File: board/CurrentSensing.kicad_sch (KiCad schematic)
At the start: 12 parts, among them U16 MLX91221KDF-ABF-025-RE, U17 MLX91221KDF-ABF-025-RE, U18 MLX91221KDF-ABF-025-RE

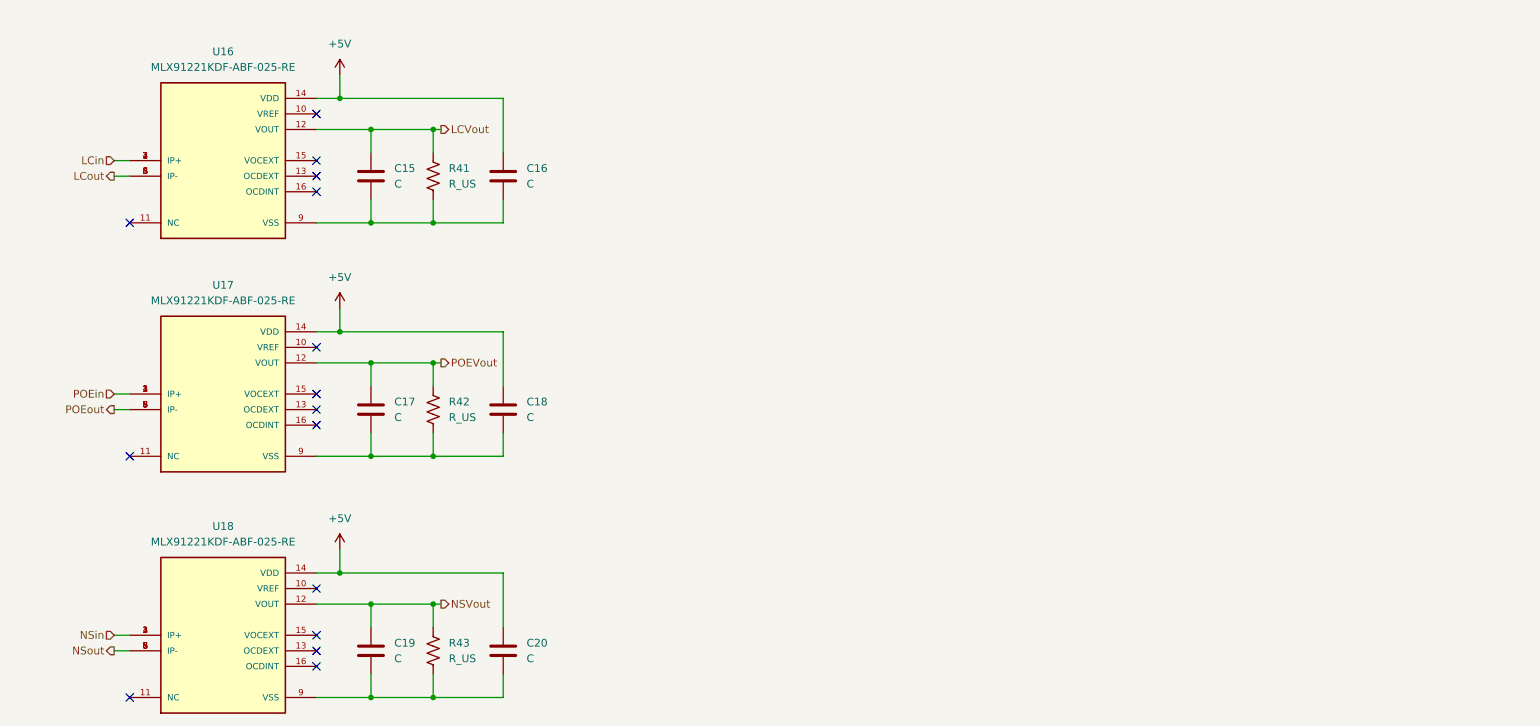
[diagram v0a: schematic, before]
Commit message: sync previous 2 commits changes correctly
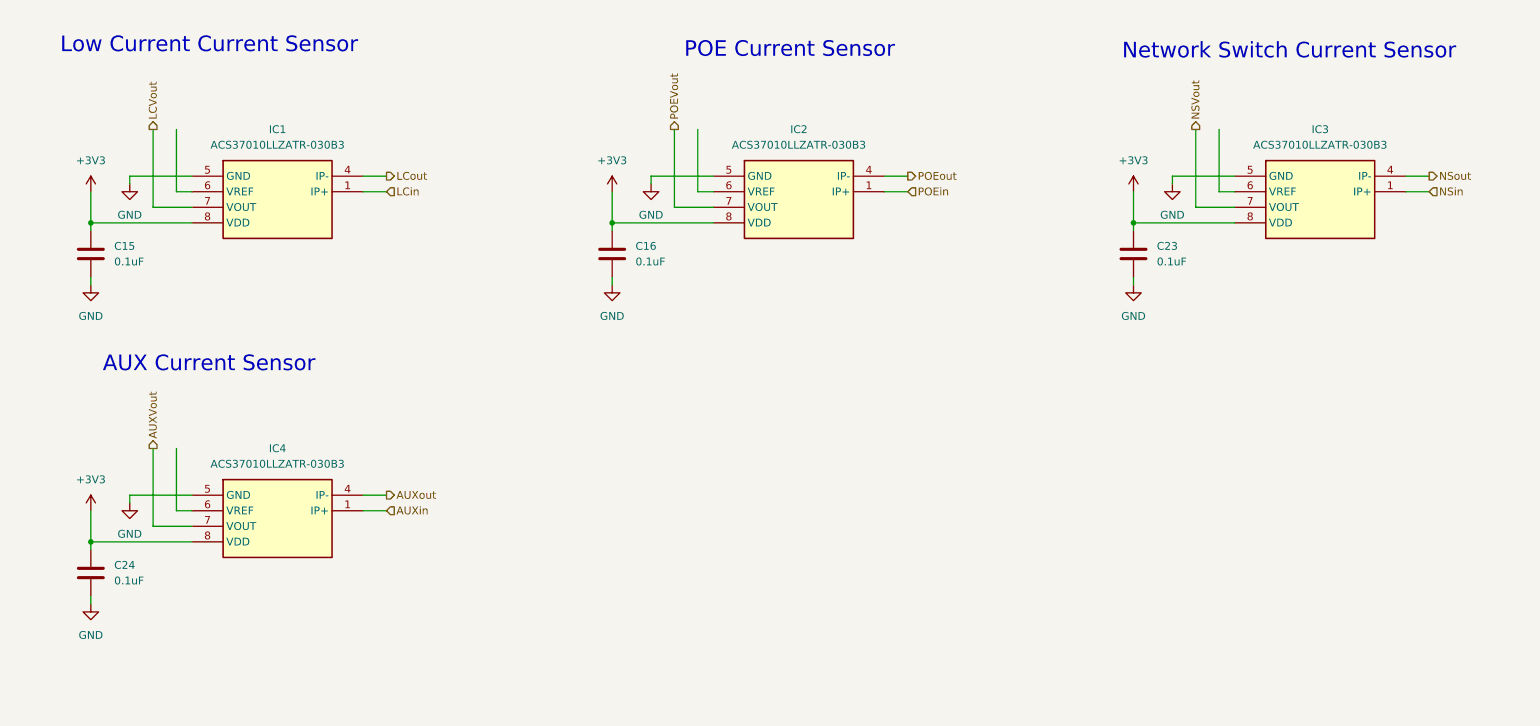
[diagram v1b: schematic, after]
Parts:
- removed C17, C18, C19, C20: C, symbol Device:C
- removed R41, R42, R43: R_US, symbol Device:R_US
- removed U16, U17, U18: MLX91221KDF-ABF-025-RE, MLX91221KDF-ABF-025-RE:SOIC127P1031X264-16N, symbol MLX91221KDF-ABF-025-RE:MLX91221KDF-ABF-025-RE
- added C23, C24: 0.1uF, symbol Device:C
- added IC1, IC2, IC3, IC4: ACS37010LLZATR-030B3, ACS37010LLZATR050B5, symbol ACS37010LLZATR-030B3:ACS37010LLZATR-030B3
- C15, C16: value C -> 0.1uF
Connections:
- net LCVout: now also IC1.7 (VOUT); no longer C15.1
- net LCin: now also IC1.1 (IP+)
- net LCout: now also IC1.4 (IP-)
- net NSVout: now also IC3.7 (VOUT)
- net NSin: now also IC3.1 (IP+)
- net NSout: now also IC3.4 (IP-)
- net POEVout: now also IC2.7 (VOUT)
- net POEin: now also IC2.1 (IP+)
- net POEout: now also IC2.4 (IP-)
- net GND: now reaches C15.2, C16.2
- net GND: now also C23.2, C24.2, IC1.5 (GND), IC2.5 (GND), IC3.5 (GND), IC4.5 (GND)
- net +5V renamed +3V3
- net +3V3: now also C15.1, C23.1, C24.1, IC1.8 (VDD), IC2.8 (VDD), IC3.8 (VDD), IC4.8 (VDD)
- new net AUXVout: IC4.7 (VOUT)
- new net AUXin: IC4.1 (IP+)
- new net AUXout: IC4.4 (IP-)
- no-connect marks 15 -> 0
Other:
- note added: "AUX Current Sensor"
- note added: "Low Current Current Sensor"
- note added: "Network Switch Current Sensor"
- note added: "POE Current Sensor"

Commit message: Created Current Sensors in Sensinator
-Create current sensors for m2, m5, m9, Low Current, Network, and AUX
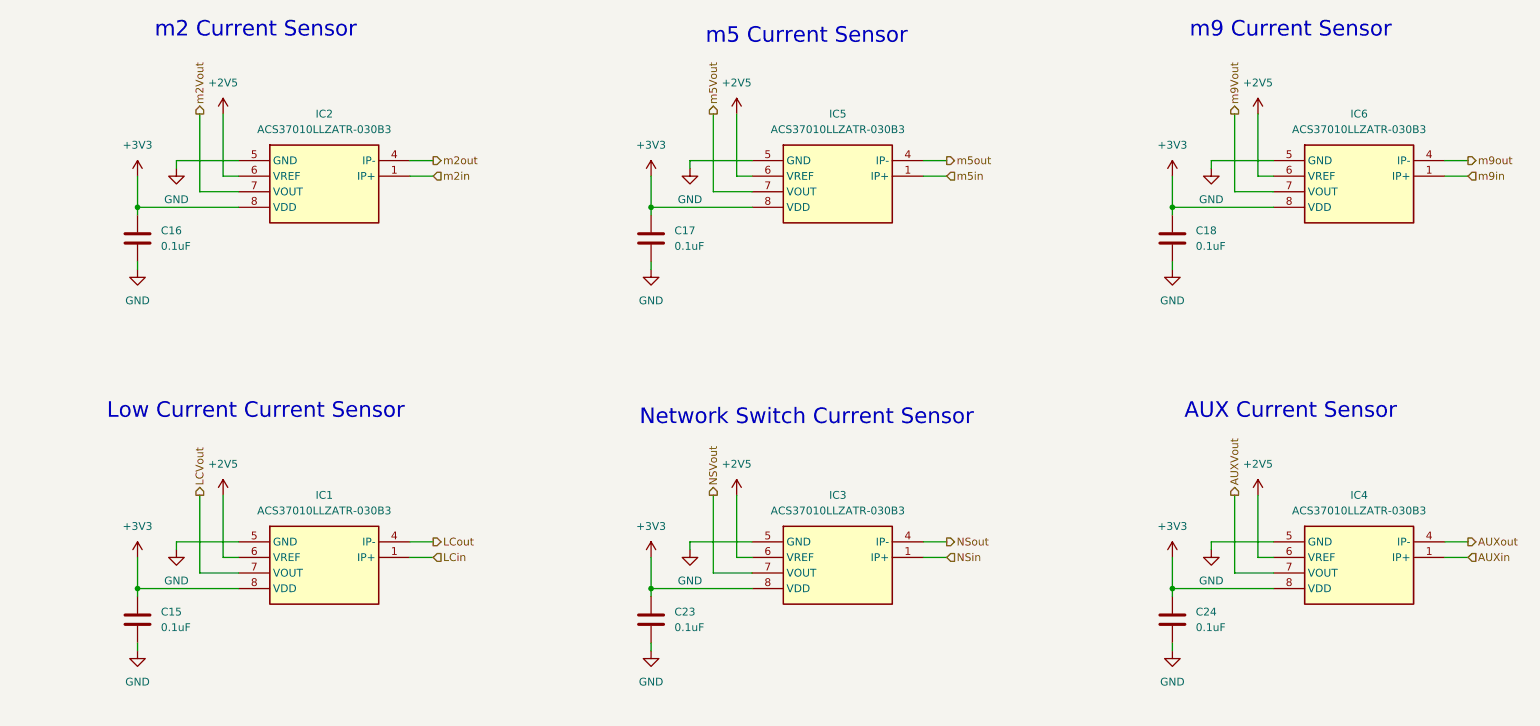
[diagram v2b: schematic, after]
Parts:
- added C17, C18: 0.1uF, symbol Device:C
- added IC5, IC6: ACS37010LLZATR-030B3, ACS37010LLZATR050B5, symbol ACS37010LLZATR-030B3:ACS37010LLZATR-030B3
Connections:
- net +3V3: now also C17.1, C18.1, IC5.8 (VDD), IC6.8 (VDD)
- net GND: now also C17.2, C18.2, IC5.5 (GND), IC6.5 (GND)
- net +2V5: now reaches IC1.6 (VREF)
- net +2V5: now also IC2.6 (VREF), IC3.6 (VREF), IC4.6 (VREF), IC5.6 (VREF), IC6.6 (VREF)
- net POEVout renamed m2Vout
- net POEin renamed m2in
- net POEout renamed m2out
- new net m5Vout: IC5.7 (VOUT)
- new net m5in: IC5.1 (IP+)
- new net m5out: IC5.4 (IP-)
- new net m9Vout: IC6.7 (VOUT)
- new net m9in: IC6.1 (IP+)
- new net m9out: IC6.4 (IP-)
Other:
- note added: "m2 Current Sensor"
- note added: "m5 Current Sensor"
- note added: "m9 Current Sensor"
- note removed: "POE Current Sensor"
- moved on the sheet: C15, C23, C24, IC1, IC3, IC4
